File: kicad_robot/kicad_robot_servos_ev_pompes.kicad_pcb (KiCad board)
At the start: 2 copper layers, 62 parts, among them J1 Conn_I2C, J10 Conn_SERVO_3, J11 Conn_SERVO_4, J12 Conn_SERVO_5, J13 Conn_EV_1, J14 Conn_EV_2, J15 Conn_EV_3, J16 Conn_EV_4, J17 Conn_EV_5, J2 Screw_Terminal_POWER, J3 Conn_POMPE_1, J4 Conn_POMPE_5, J5 Conn_POMPE_2, J6 Conn_POMPE_3, J7 Conn_POMPE_4, J8 Conn_SERVO_1, J9 Conn_SERVO_2, Q1 IRLML0030, Q10 IRLML0030, Q2 IRLML0030, Q3 IRLML0030, Q4 IRLML0030, Q5 IRLML0030, Q6 IRLML0030, Q7 IRLML0030, Q8 IRLML0030, Q9 IRLML0030, U1 TSR_1-2450, U2 LM3940, U3 ADC128D818, U4 PCA9685PW, U5 ACS722xLCTR-05AB, U6 ACS722xLCTR-05AB, U7 ACS722xLCTR-05AB, U8 ACS722xLCTR-05AB, U9 ACS722xLCTR-05AB

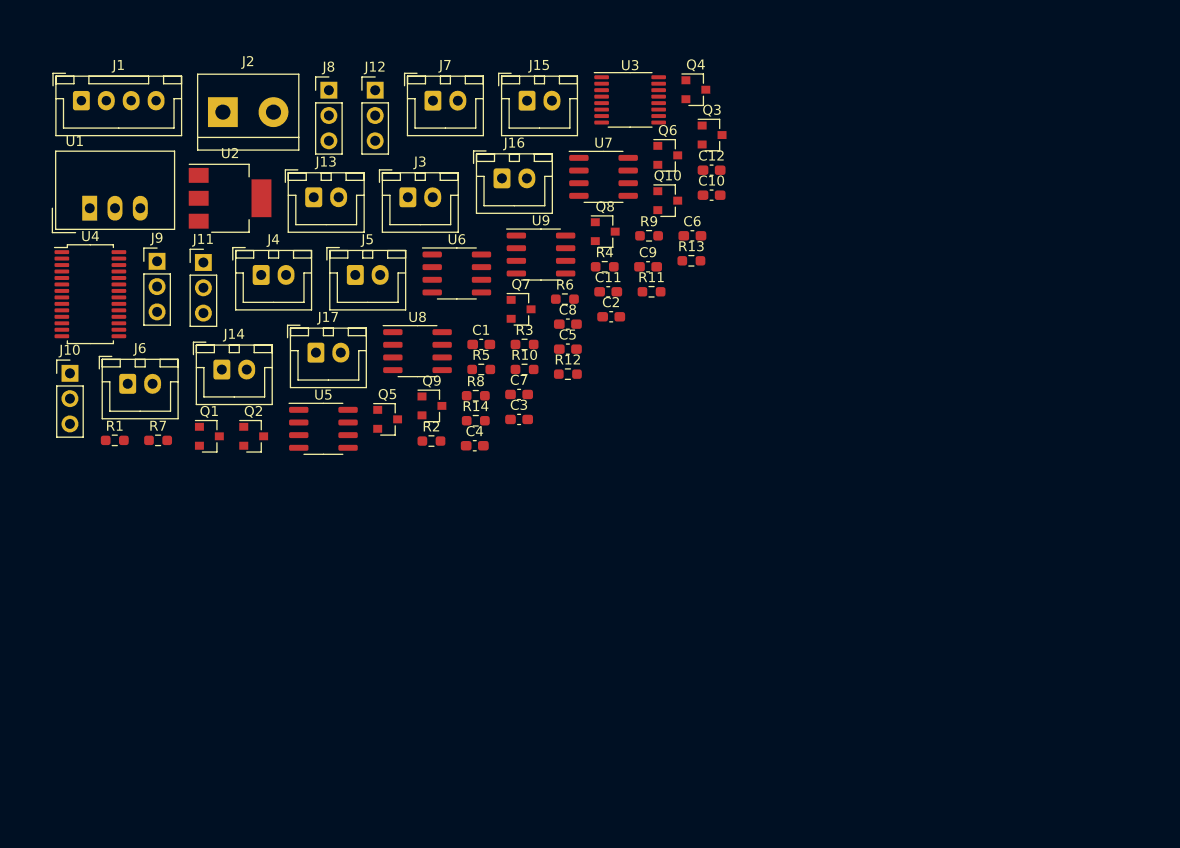
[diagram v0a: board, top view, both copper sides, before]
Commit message: Placement des composants
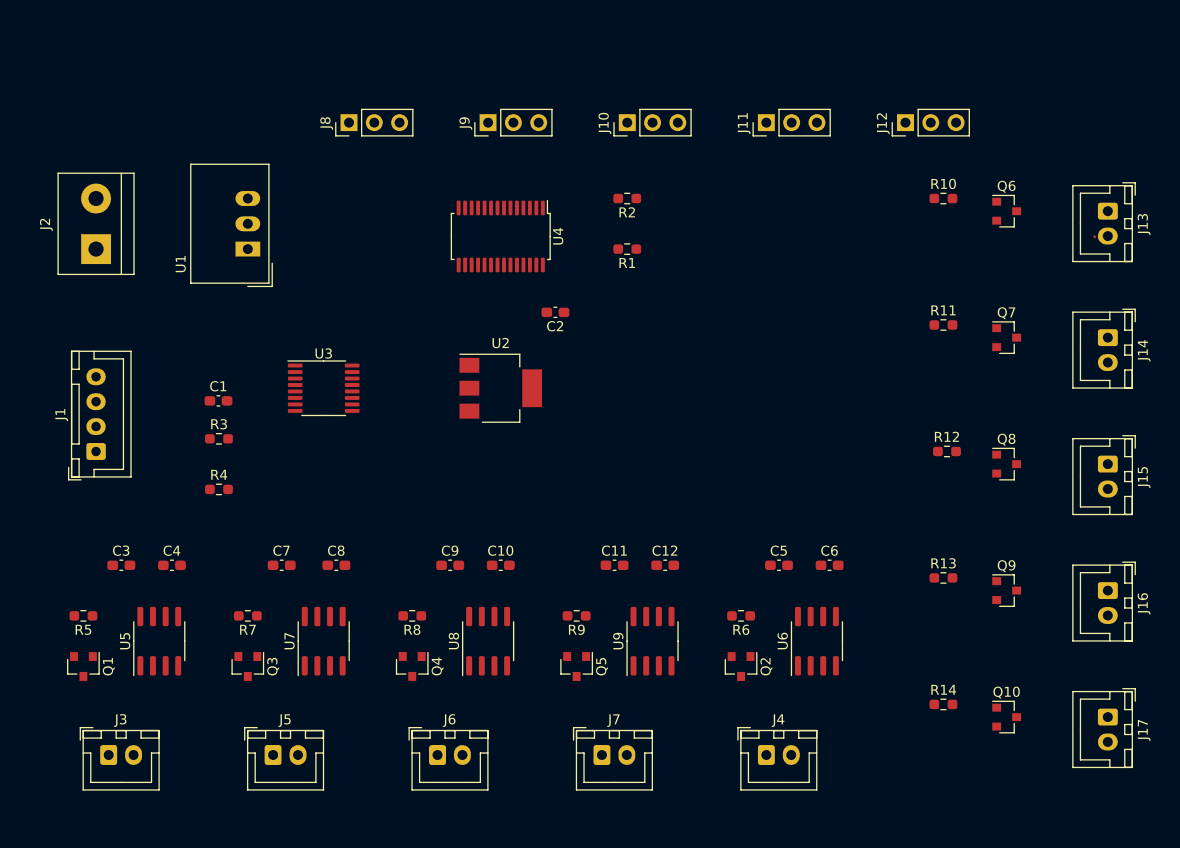
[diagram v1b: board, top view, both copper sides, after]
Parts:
- moved J14 89.0 mm to (121.9, 43.2), turned to 270 degrees
- moved J17 87.5 mm to (121.9, 81.3), turned to 270 degrees
- moved J13 79.8 mm to (121.9, 30.5), turned to 270 degrees
- moved J16 73.6 mm to (121.9, 68.6), turned to 270 degrees
- moved Q3 70.9 mm to (35.6, 76.2), turned to 270 degrees
- moved J4 70.0 mm to (87.6, 85.1)
- moved J15 68.8 mm to (121.9, 55.9), turned to 270 degrees
- moved J7 67.9 mm to (71.1, 85.1)
- moved Q4 64.5 mm to (52.1, 76.2), turned to 270 degrees
- moved J3 63.6 mm to (21.6, 85.1)
- moved Q10 62.0 mm to (111.8, 81.3)
- moved J10 61.4 mm to (73.7, 21.6), turned to 90 degrees
- moved Q9 60.6 mm to (111.8, 68.6)
- moved J11 58.2 mm to (87.6, 21.6), turned to 90 degrees
- moved R1 54.9 mm to (73.7, 34.3), turned to 180 degrees
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
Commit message: Réarrangement des composants / Routage (v1)
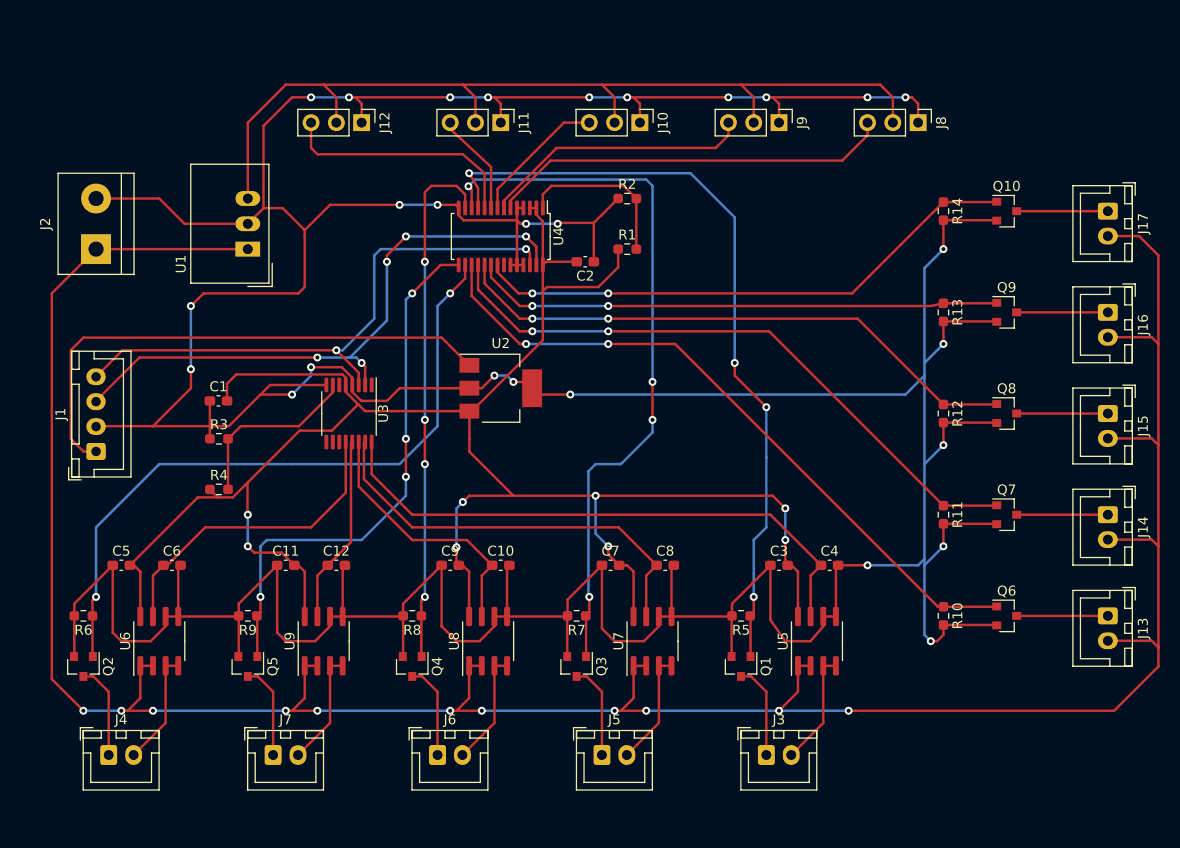
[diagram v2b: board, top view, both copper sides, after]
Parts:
- moved C3 66.0 mm to (88.9, 66.0)
- moved C4 66.0 mm to (94.0, 66.0)
- moved C5 66.0 mm to (22.9, 66.0)
- moved C6 66.0 mm to (27.9, 66.0)
- moved Q1 66.0 mm to (85.1, 76.2)
- moved Q2 66.0 mm to (19.1, 76.2)
- moved R5 66.0 mm to (85.1, 71.1)
- moved R6 66.0 mm to (19.1, 71.1)
- moved J3 66.0 mm to (87.6, 85.1)
- moved J4 66.0 mm to (21.6, 85.1)
- moved U5 66.0 mm to (92.7, 73.7)
- moved U6 66.0 mm to (26.7, 73.7)
- moved J8 57.2 mm to (102.9, 21.6), turned to 270 degrees
- moved J12 54.6 mm to (47.0, 21.6), turned to 270 degrees
- moved J17 50.8 mm to (121.9, 30.5)
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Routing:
- net GND: track 0.00 -> 568.9 mm, vias 0 -> 27
- net +12V: track 0.00 -> 274.9 mm, vias 0 -> 11
- net +3V3: track 0.00 -> 203.3 mm, vias 0 -> 8
- net +5V: track 0.00 -> 94.4 mm
- net /POMPE_1: track 0.00 -> 78.3 mm, vias 0 -> 4
- net /POMPE_2: track 0.00 -> 73.0 mm, vias 0 -> 4
- net /POMPE_5: track 0.00 -> 69.0 mm, vias 0 -> 2
- net /EV_1: track 0.00 -> 68.8 mm, vias 0 -> 2
- net /EV_2: track 0.00 -> 63.6 mm, vias 0 -> 2
- net /EXT_SDA: track 0.00 -> 61.0 mm, vias 0 -> 5
- net /EXT_SCL: track 0.00 -> 58.4 mm, vias 0 -> 2
- net /EV_3: track 0.00 -> 58.3 mm, vias 0 -> 2
- net /ADC_1: track 0.00 -> 57.7 mm
- net /EV_5: track 0.00 -> 55.6 mm, vias 0 -> 2
- net /POMPE_4: track 0.00 -> 54.4 mm, vias 0 -> 4
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
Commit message: Ajout de sérigraphie pour repérer les numéros d'équipements facilement sur la carte
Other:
- board text added: "12V"
- board text added: "EV 1"
- board text added: "EV 2"
- board text added: "EV 3"
- board text added: "EV 4"
- board text added: "EV 5"
- board text added: "GND"
- board text added: "Pompe 1"
- board text added: "Pompe 2"
- board text added: "Pompe 3"
- board text added: "Pompe 4"
- board text added: "Pompe 5"
- board text added: "Servo 1"
- board text added: "Servo 2"
- board text added: "Servo 3"
- board text added: "Servo 4"
- board text added: "Servo 5"
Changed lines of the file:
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@@
   (general
     (thickness 1.6)
-    (drawings 0)
+    (drawings 17)
     (tracks 662)
     (zones 0)
@@
     )
   )
+  (gr_text GND (at 14.605 28.575 270) (layer F.SilkS)
+    (effects (font (size 1.5 1.5) (thickness 0.3)))
+  )
+  (gr_text 12V (at 14.605 34.925 270) (layer F.SilkS)
+    (effects (font (size 1.5 1.5) (thickness 0.3)))
+  )
+  (gr_text "EV 1" (at 114.3 75.565) (layer F.SilkS)
+    (effects (font (size 1.5 1.5) (thickness 0.3)))
+  )
+  (gr_text "EV 2" (at 114.3 65.405) (layer F.SilkS)
+    (effects (font (size 1.5 1.5) (thickness 0.3)))
+  )
+  (gr_text "EV 3" (at 114.3 55.245) (layer F.SilkS)
+    (effects (font (size 1.5 1.5) (thickness 0.3)))
+  )
+  (gr_text "EV 4" (at 114.3 45.085) (layer F.SilkS)
+    (effects (font (size 1.5 1.5) (thickness 0.3)))
+  )
+  (gr_text "EV 5" (at 114.3 34.925) (layer F.SilkS)
+    (effects (font (size 1.5 1.5) (thickness 0.3)))
+  )
+  (gr_text "Pompe 5" (at 22.86 90.805) (layer F.SilkS)
+    (effects (font (size 1.5 1.5) (thickness 0.3)))
+  )
+  (gr_text "Pompe 4" (at 39.37 90.805) (layer F.SilkS)
+    (effects (font (size 1.5 1.5) (thickness 0.3)))
+  )
+  (gr_text "Pompe 3" (at 55.88 90.805) (layer F.SilkS)
+    (effects (font (size 1.5 1.5) (thickness 0.3)))
+  )
+  (gr_text "Pompe 2" (at 72.39 90.805) (layer F.SilkS)
+    (effects (font (size 1.5 1.5) (thickness 0.3)))
+  )
+  (gr_text "Pompe 1" (at 88.9 90.805) (layer F.SilkS)
+    (effects (font (size 1.5 1.5) (thickness 0.3)))
+  )
+  (gr_text "Servo 5" (at 44.45 16.51) (layer F.SilkS)
+    (effects (font (size 1.5 1.5) (thickness 0.3)))
+  )
+  (gr_text "Servo 4" (at 58.42 16.51) (layer F.SilkS)
+    (effects (font (size 1.5 1.5) (thickness 0.3)))
+  )
+  (gr_text "Servo 3" (at 72.39 16.51) (layer F.SilkS)
+    (effects (font (size 1.5 1.5) (thickness 0.3)))
+  )
+  (gr_text "Servo 2" (at 86.36 16.51) (layer F.SilkS)
+    (effects (font (size 1.5 1.5) (thickness 0.3)))
+  )
+  (gr_text "Servo 1" (at 100.33 16.51) (layer F.SilkS)
+    (effects (font (size 1.5 1.5) (thickness 0.3)))
+  )
   (segment (start 24.765 71.185) (end 24.765 66.675) (width 0.25) (layer F.Cu) (net 1))

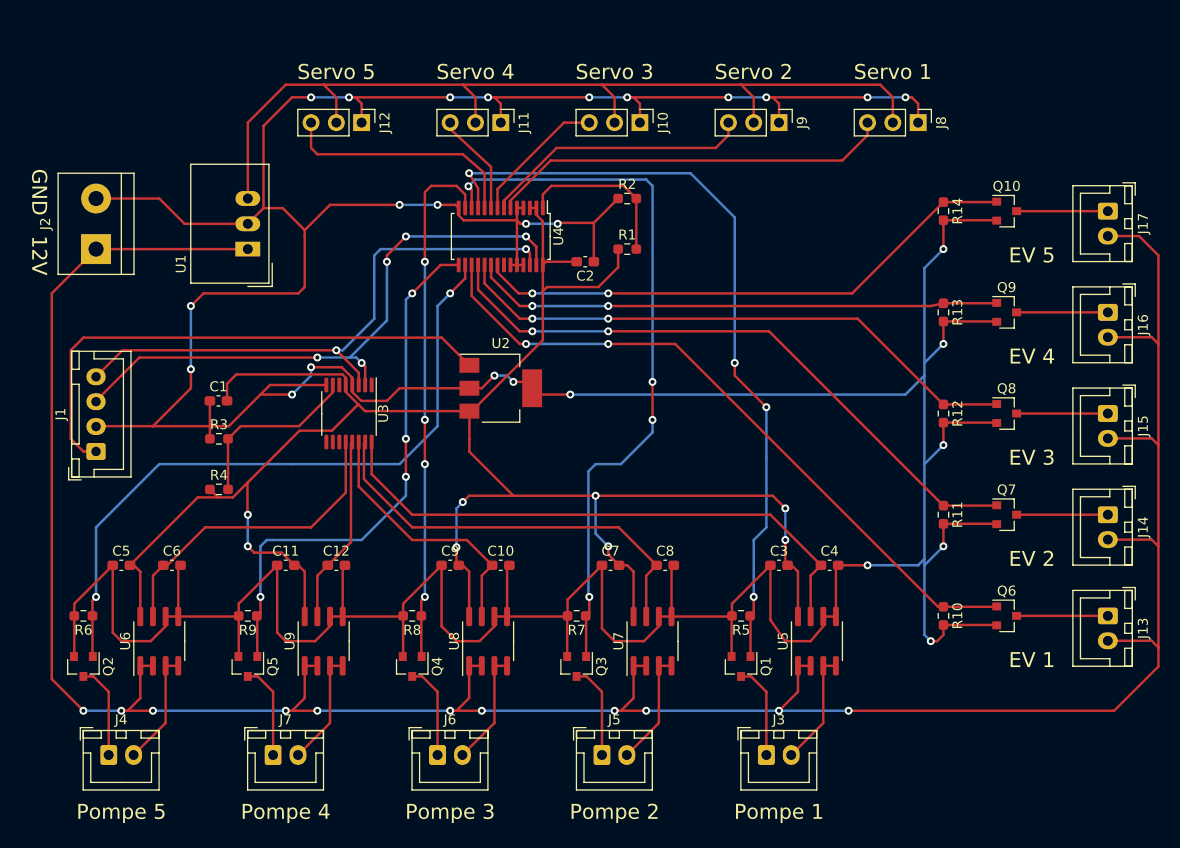
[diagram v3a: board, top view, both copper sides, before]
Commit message: Routage V2 de la carte servos/ev/pompes
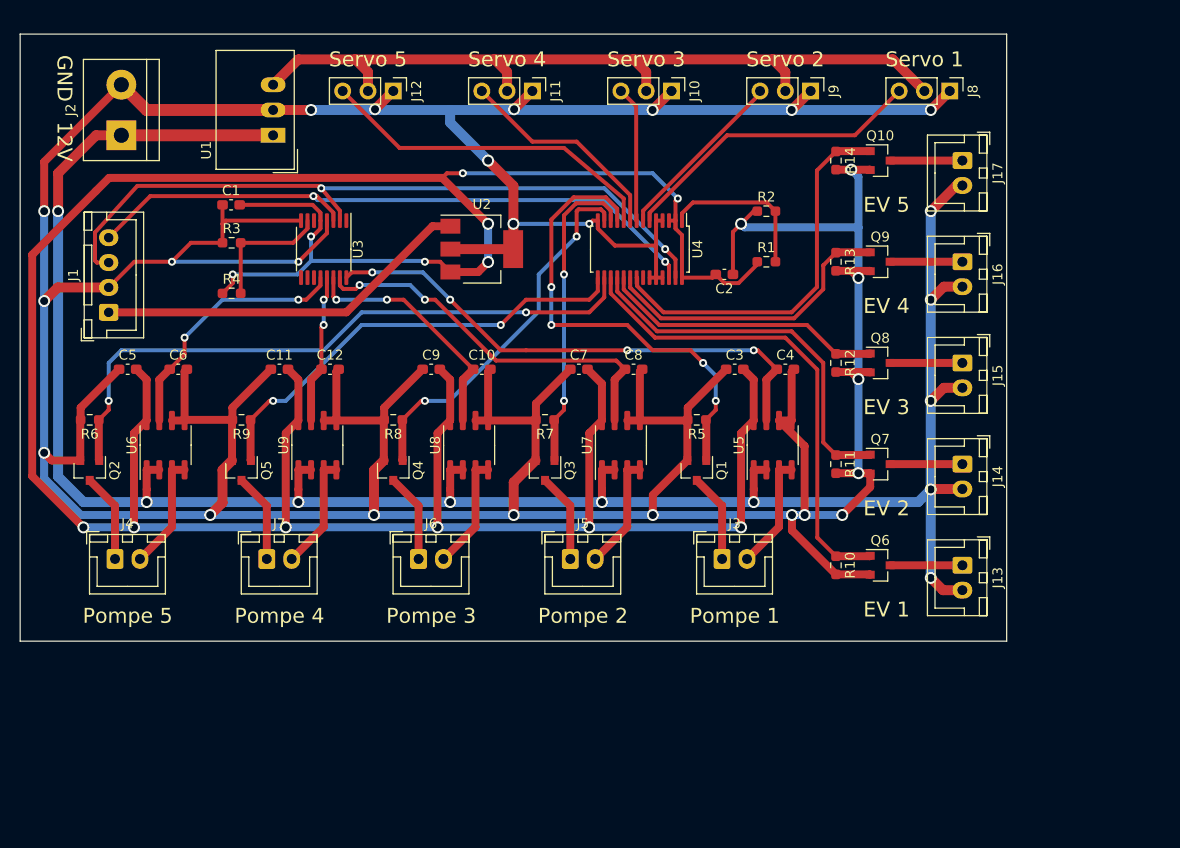
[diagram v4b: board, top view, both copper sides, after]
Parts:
- moved C3 20.2 mm to (84.5, 46.4)
- moved C4 20.2 mm to (89.5, 46.4)
- moved Q1 20.2 mm to (80.6, 56.5)
- moved R5 20.2 mm to (80.6, 51.4)
- moved J3 20.2 mm to (83.2, 65.4)
- moved U5 20.2 mm to (88.3, 54.0)
- moved C7 19.9 mm to (68.8, 46.4)
- moved C8 19.9 mm to (74.3, 46.4)
- moved J5 19.9 mm to (67.9, 65.4)
- moved Q3 19.9 mm to (65.4, 56.5)
- moved R7 19.9 mm to (65.4, 51.4)
- moved U7 19.9 mm to (73.0, 54.0)
- moved C10 19.8 mm to (59.1, 46.4)
- moved C9 19.8 mm to (54.0, 46.4)
- moved J6 19.8 mm to (52.7, 65.4)
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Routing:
- net +3V3: track 203.3 -> 320.7 mm, vias 8 -> 13
- net +12V: track 274.9 -> 220.8 mm
- net /POMPE_2: track 73.0 -> 31.5 mm, vias 4 -> 2
- net /POMPE_1: track 78.3 -> 47.4 mm
- net /EV_3: track 58.3 -> 28.6 mm, vias 2 -> 0
- net /EV_2: track 63.6 -> 38.3 mm, vias 2 -> 0
- net GND: track 568.9 -> 545.1 mm, vias 27 -> 26
- net /EV_4: track 53.8 -> 30.5 mm, vias 2 -> 0
- net /EV_1: track 68.8 -> 48.5 mm, vias 2 -> 0
- net /EV_5: track 55.6 -> 38.9 mm, vias 2 -> 0
- net +5VA: track 53.7 -> 37.9 mm
- net /POMPE_3: track 52.8 -> 37.7 mm, vias 4 -> 2
- net /EXT_SDA: track 61.0 -> 73.5 mm, vias 5 -> 2
- net +5V: track 94.4 -> 82.6 mm
- net /SERVO_4: track 10.4 -> 21.8 mm
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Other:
- board outline added: 99.1 x 61 mm

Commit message: Routage Carte Servos/EV/Pompes v3 (avec mounting holes)
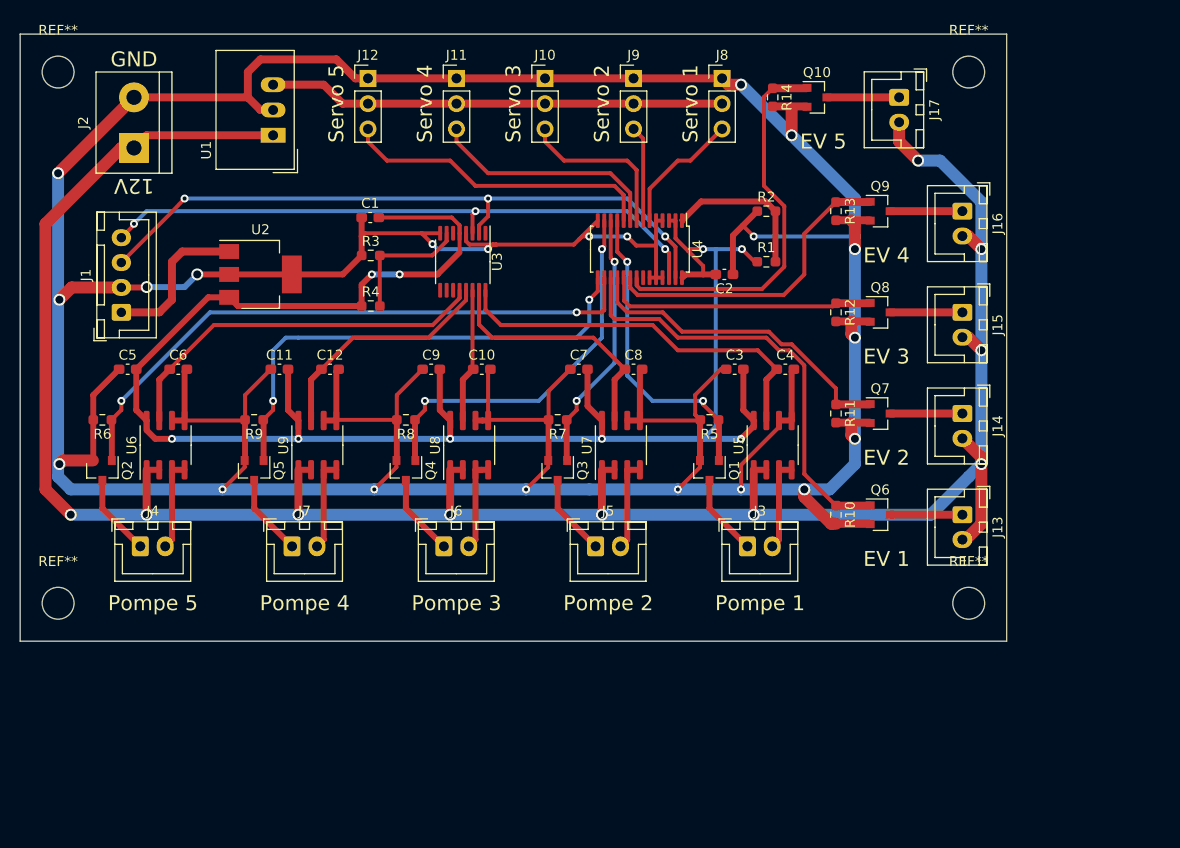
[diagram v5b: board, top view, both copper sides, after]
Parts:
- added REF**: MountingHole_3.2mm_M3, MountingHole:MountingHole_3.2mm_M3, F.Cu at (16.5, 16.5)
- added REF**: MountingHole_3.2mm_M3, MountingHole:MountingHole_3.2mm_M3, F.Cu at (16.5, 69.8)
- added REF**: MountingHole_3.2mm_M3, MountingHole:MountingHole_3.2mm_M3, F.Cu at (108.0, 69.8)
- added REF**: MountingHole_3.2mm_M3, MountingHole:MountingHole_3.2mm_M3, F.Cu at (108.0, 16.5)
- moved J8 22.9 mm to (83.2, 17.1), turned to 0 degrees
- moved U2 22.4 mm to (36.8, 36.8)
- moved J9 17.8 mm to (74.3, 17.1), turned to 0 degrees
- moved R3 14.0 mm to (47.9, 34.9)
- moved R4 14.0 mm to (47.9, 40.0)
- moved C1 14.0 mm to (47.9, 31.1)
- moved U3 14.0 mm to (57.1, 35.6)
- moved J10 12.8 mm to (65.4, 17.1), turned to 0 degrees
- moved Q10 8.98 mm to (92.7, 19.1)
- moved J17 8.98 mm to (101.0, 19.1)
- moved R14 8.98 mm to (88.3, 19.1)
- moved J11 7.73 mm to (56.5, 17.1), turned to 0 degrees
- moved J13 5.08 mm to (107.3, 61.0)
- moved J14 5.08 mm to (107.3, 50.8)
- moved Q6 5.08 mm to (99.1, 61.0)
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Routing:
- net +3V3: track 320.7 -> 185.2 mm, vias 13 -> 9
- net GND: track 545.1 -> 503.9 mm, vias 26 -> 21
- net +5V: track 82.6 -> 45.9 mm
- net +5VA: track 37.9 -> 15.6 mm
- net /SERVO_1: track 30.9 -> 13.0 mm
- net /POMPE_1: track 47.4 -> 31.3 mm, vias 4 -> 2
- net +12V: track 220.8 -> 235.1 mm, vias 11 -> 10
- net /ADC_1: track 53.0 -> 39.3 mm, vias 4 -> 0
- net /ADC_2: track 38.8 -> 25.5 mm, vias 2 -> 0
- net /ADC_5: track 26.0 -> 38.4 mm, vias 2 -> 0
- net /ADC_3: track 24.6 -> 13.5 mm, vias 2 -> 0
- net /ADC_4: track 15.0 -> 24.0 mm, vias 2 -> 0
- net /SERVO_2: track 17.9 -> 9.60 mm
- net /EXT_SDA: track 73.5 -> 67.3 mm, vias 2 -> 3
- net /POMPE_2: track 31.5 -> 26.3 mm
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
